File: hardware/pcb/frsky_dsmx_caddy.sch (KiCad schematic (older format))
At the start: 28 parts, among them P1 G9X, P2 Fr-Sky, P3 DSMX, Q1 BC847C, Q2 Si2319DS, Q3 Si2319DS, Q4 BC847C, U1 78L05, U2 LN-6206-30

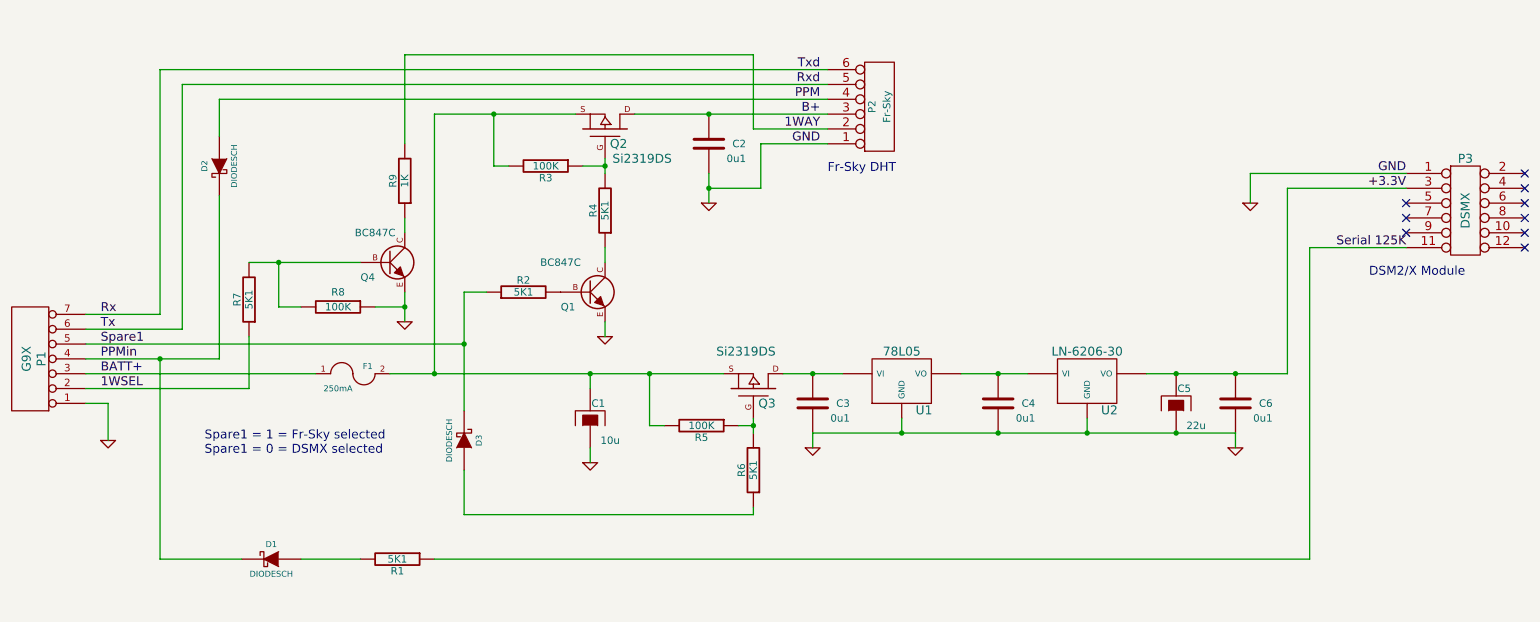
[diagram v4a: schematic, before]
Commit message: TX_caddy design fault corrected (and tested.)
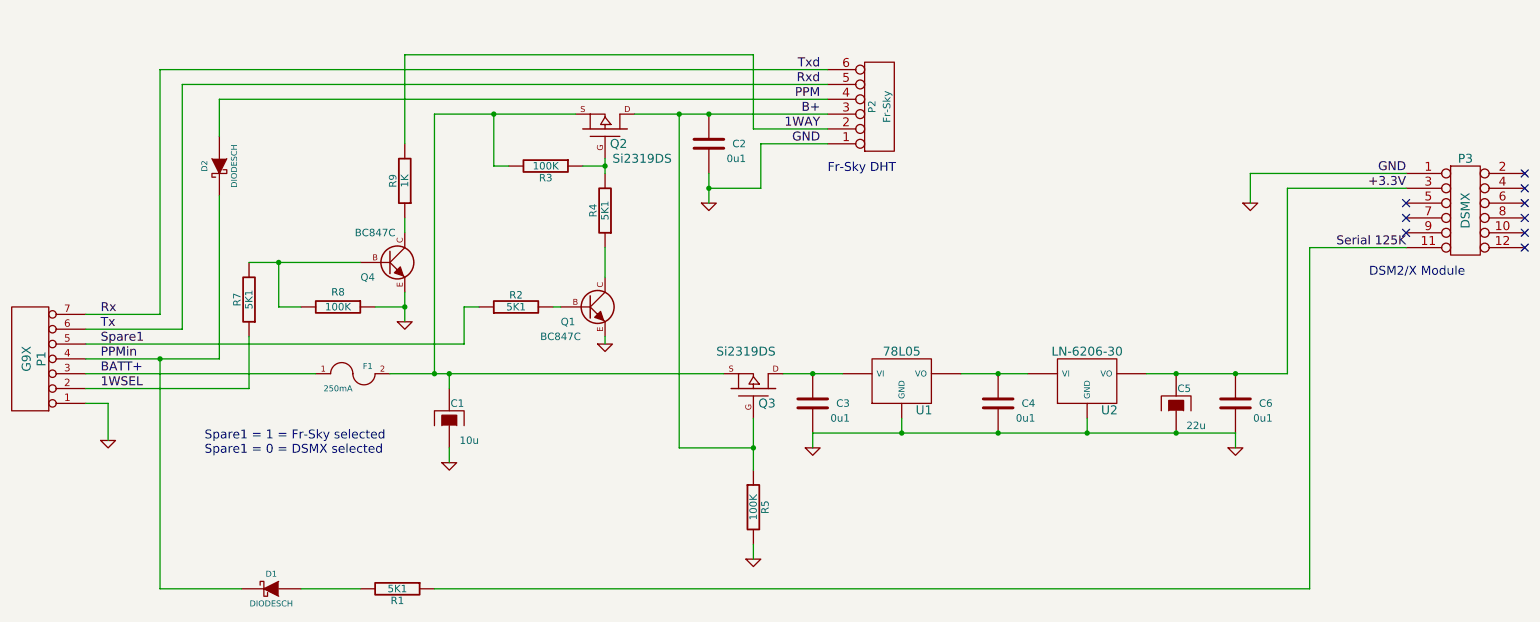
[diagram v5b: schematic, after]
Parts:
- removed D3: DIODESCH, symbol DIODESCH
- removed R6: 5K1, symbol R
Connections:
- net B+: now also Q3.G, R5.1
- net GND: now also R5.2
- net at C1.2, F1.2, Q2.S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: no longer R5.2
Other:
- moved on the sheet: C1, D1, Q1, R1, R2
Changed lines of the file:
@@
-EESchema Schematic File Version 2  date Wed 26 Sep 2012 04:29:42 PM NZST
+EESchema Schematic File Version 2  date Wed 24 Oct 2012 07:34:05 PM NZDT
 LIBS:gruvin
 LIBS:power
@@
 Sheet 1 1
 Title "Fr-Sky / DSMX TX Moudle Caddy"
-Date "26 sep 2012"
-Rev "1.2"
+Date "24 oct 2012"
+Rev "1.3"
 Comp ""
 Comment1 ""
@@
 Comment4 "Licensed under the TAPR Open Hardware License (see file,  LICENSE)"
 $EndDescr
-Text Label 1350 3600 0    60   ~ 0
-1WSEL
+Wire Wire Line
+	5750 4750 5750 4650
+Connection ~ 5250 1750
+Wire Wire Line
+	5250 1750 5250 4000
+Wire Wire Line
+	4750 2650 4750 2850
+Wire Wire Line
+	4750 3250 4750 3300
+Wire Wire Line
+	3800 3050 3800 3300
 Connection ~ 2550 2750
 Wire Wire Line
-	2550 3050 2550 2750
+	2550 2750 2550 3050
 Wire Wire Line
 	2550 3050 2700 3050
 Wire Wire Line
-	3100 2750 2350 2750
+	2350 2750 2550 2750
+Wire Wire Line
+	2550 2750 3100 2750
 Wire Wire Line
 	2350 3250 2350 3600
@@
 	2350 3600 1250 3600
 Wire Wire Line
-	3600 4750 9500 4750
-Wire Wire Line
-	9500 4750 9500 2650
+	3600 4950 9500 4950
+Wire Wire Line
+	9500 4950 9500 2650
 Wire Wire Line
 	9500 2650 10150 2650
-Connection ~ 3800 3300
-Wire Wire Line
-	3800 3750 3800 2950
-Wire Wire Line
-	3800 2950 3950 2950
-Wire Wire Line
-	1250 3300 3800 3300
-Wire Wire Line
-	5450 2150 5450 2350
+Wire Wire Line
+	3800 3050 3900 3050
+Wire Wire Line
+	3800 3300 1250 3300
+Wire Wire Line
+	5450 2350 5450 2250
+Wire Wire Line
+	5450 2250 5450 2150
 Connection ~ 5450 2250
 Wire Wire Line
-	6150 3900 6150 4000
-Wire Wire Line
-	9000 3900 9000 4000
-Wire Wire Line
-	4650 4000 4650 4100
-Wire Wire Line
-	1750 4750 1750 3400
-Wire Wire Line
-	1750 4750 2300 4750
+	6150 4000 6150 3900
+Wire Wire Line
+	9000 4000 9000 3900
+Wire Wire Line
+	3700 4000 3700 4100
+Wire Wire Line
+	1750 3400 1750 4950
+Wire Wire Line
+	1750 4950 2300 4950
 Connection ~ 8600 3900
 Connection ~ 8600 3500
 Connection ~ 9000 3500
 Wire Wire Line
-	6150 3900 9000 3900
+	9000 3900 8600 3900
+Wire Wire Line
+	8600 3900 8000 3900
+Wire Wire Line
+	8000 3900 7400 3900
+Wire Wire Line
+	7400 3900 6750 3900
+Wire Wire Line
+	6750 3900 6150 3900
 Connection ~ 1750 3400
 Wire Wire Line
-	2150 3400 2150 2300
+	2150 2300 2150 3400
 Wire Wire Line
 	10150 2150 9100 2150
@@
 	9100 2150 9100 2350
 Wire Wire Line
-	4450 2950 4450 2950
-Wire Wire Line
-	4750 2750 4750 2650
-Wire Wire Line
 	6250 1450 1750 1450
 Wire Wire Line
@@
 Wire Wire Line
 	1250 3500 2800 3500
-Connection ~ 5750 3850
-Wire Wire Line
-	5650 3850 5750 3850
-Connection ~ 4650 3500
-Wire Wire Line
-	7600 3500 7150 3500
-Wire Wire Line
-	4650 3500 4650 3600
-Wire Wire Line
-	8400 3500 9350 3500
-Wire Wire Line
-	4550 1750 3600 1750
-Wire Wire Line
-	4750 2050 4750 2150
+Connection ~ 3700 3500
+Wire Wire Line
+	7150 3500 7400 3500
+Wire Wire Line
+	7400 3500 7600 3500
+Wire Wire Line
+	3700 3500 3700 3600
+Wire Wire Line
+	8400 3500 8600 3500
+Wire Wire Line
+	8600 3500 9000 3500
+Wire Wire Line
+	9000 3500 9350 3500
+Wire Wire Line
+	4550 1750 4000 1750
+Wire Wire Line
+	4000 1750 3600 1750
+Wire Wire Line
+	4750 2150 4750 2100
+Wire Wire Line
+	4750 2100 4750 2050
 Connection ~ 6750 3900
-Wire Wire Line
-	4750 3150 4750 3250
 Connection ~ 6150 3500
 Connection ~ 7400 3900
 Wire Wire Line
-	6250 1750 4950 1750
+	4950 1750 5250 1750
+Wire Wire Line
+	5250 1750 5450 1750
+Wire Wire Line
+	5450 1750 6250 1750
 Wire Wire Line
 	8000 3900 8000 3800
 Connection ~ 7400 3500
 Wire Wire Line
-	5750 3900 5750 3800
-Wire Wire Line
-	5750 4450 3800 4450
-Wire Wire Line
-	5750 4450 5750 4400
-Wire Wire Line
 	3600 1750 3600 3500
 Connection ~ 3600 3500
@@
 Connection ~ 4750 2100
 Wire Wire Line
-	3300 3500 5550 3500
-Wire Wire Line
 	6250 1650 2150 1650
 Wire Wire Line
-	1250 3400 2150 3400
+	2150 3400 1750 3400
+Wire Wire Line
+	1750 3400 1250 3400
 Wire Wire Line
 	6250 1550 1900 1550
@@
 	2150 1650 2150 1900
 Wire Wire Line
-	6350 3500 5950 3500
-Wire Wire Line
-	3100 4750 2700 4750
+	5950 3500 6150 3500
+Wire Wire Line
+	6150 3500 6350 3500
+Wire Wire Line
+	3100 4950 2700 4950
 Wire Wire Line
 	1250 3700 1400 3700
@@
 	5800 2250 5800 1950
 Wire Wire Line
-	5150 3850 5050 3850
-Wire Wire Line
-	5050 3850 5050 3500
-Connection ~ 5050 3500
-Wire Wire Line
 	4100 2100 4000 2100
 Wire Wire Line
@@
 Connection ~ 4000 1750
 Wire Wire Line
-	3800 4450 3800 4150
-Wire Wire Line
 	5800 1950 6250 1950
 Wire Wire Line
-	3400 2950 3400 3150
+	3400 3150 3400 3050
+Wire Wire Line
+	3400 3050 3400 2950
 Wire Wire Line
 	3400 2550 3400 2450
@@
 	3200 3050 3400 3050
 Connection ~ 3400 3050
+Wire Wire Line
+	5550 3500 3700 3500
+Wire Wire Line
+	3700 3500 3600 3500
+Wire Wire Line
+	3600 3500 3300 3500
+Wire Wire Line
+	4450 3050 4400 3050
+Wire Wire Line
+	5750 4150 5750 4000
+Wire Wire Line
+	5750 4000 5750 3800
+Wire Wire Line
+	5250 4000 5750 4000
+Connection ~ 5750 4000
+$Comp
+L GND #PWR?
+U 1 1 50878285
+P 5750 4750
+F 0 "#PWR?" H 5750 4750 30  0001 C CNN
+F 1 "GND" H 5750 4680 30  0001 C CNN
+	1    5750 4750
+	1    0    0    -1
+$EndComp
+$Comp
+L R R5
+U 1 1 50877F34
+P 5750 4400
+F 0 "R5" V 5830 4400 50  0000 C CNN
+F 1 "100K" V 5750 4400 50  0000 C CNN
+	1    5750 4400
+	1    0    0    -1
+$EndComp
+Text Label 1350 3600 0    60   ~ 0
+1WSEL
 $Comp
 L BC847C Q4
@@
 $EndComp
 $Comp
-L GND #PWR01
+L GND #PWR2
 U 1 1 50627C0D
 P 3400 3150
-F 0 "#PWR01" H 3400 3150 30  0001 C CNN
+F 0 "#PWR2" H 3400 3150 30  0001 C CNN
 F 1 "GND" H 3400 3080 30  0001 C CNN
 	1    3400 3150
@@
 NoConn ~ 10150 2550
 $Comp
-L GND #PWR02
+L GND #PWR8
 U 1 1 504D1983
 P 9000 4000
-F 0 "#PWR02" H 9000 4000 30  0001 C CNN
+F 0 "#PWR8" H 9000 4000 30  0001 C CNN
 F 1 "GND" H 9000 3930 30  0001 C CNN
 	1    9000 4000
@@
 $EndComp
 $Comp
-L GND #PWR03
+L GND #PWR3
 U 1 1 504D1897
-P 4650 4100
-F 0 "#PWR03" H 4650 4100 30  0001 C CNN
-F 1 "GND" H 4650 4030 30  0001 C CNN
-	1    4650 4100
+P 3700 4100
+F 0 "#PWR3" H 3700 4100 30  0001 C CNN
+F 1 "GND" H 3700 4030 30  0001 C CNN
+	1    3700 4100
 	1    0    0    -1
 $EndComp
@@
 L DIODESCH D1
 U 1 1 504D150C
-P 2500 4750
-F 0 "D1" H 2500 4850 40  0000 C CNN
-F 1 "DIODESCH" H 2500 4650 40  0000 C CNN
-	1    2500 4750
+P 2500 4950
+F 0 "D1" H 2500 5050 40  0000 C CNN
+F 1 "DIODESCH" H 2500 4850 40  0000 C CNN
+	1    2500 4950
 	-1   0    0    -1
 $EndComp
@@
 L R R1
 U 1 1 504D1401
-P 3350 4750
-F 0 "R1" V 3430 4750 50  0000 C CNN
-F 1 "5K1" V 3350 4750 50  0000 C CNN
-	1    3350 4750
+P 3350 4950
+F 0 "R1" V 3430 4950 50  0000 C CNN
+F 1 "5K1" V 3350 4950 50  0000 C CNN
+	1    3350 4950
 	0    1    1    0
 $EndComp
 $Comp
-L GND #PWR04
+L GND #PWR9
 U 1 1 504D13B3
 P 9100 2350
-F 0 "#PWR04" H 9100 2350 30  0001 C CNN
+F 0 "#PWR9" H 9100 2350 30  0001 C CNN
 F 1 "GND" H 9100 2280 30  0001 C CNN
 	1    9100 2350
@@
 PPMin
 $Comp
-L GND #PWR05
+L GND #PWR5
 U 1 1 504D1165
 P 5450 2350
-F 0 "#PWR05" H 5450 2350 30  0001 C CNN
+F 0 "#PWR5" H 5450 2350 30  0001 C CNN
 F 1 "GND" H 5450 2280 30  0001 C CNN
 	1    5450 2350
@@
 BATT+
 $Comp
-L GND #PWR06
+L GND #PWR1
 U 1 1 504D1086
 P 1400 3950
-F 0 "#PWR06" H 1400 3950 30  0001 C CNN
+F 0 "#PWR1" H 1400 3950 30  0001 C CNN
 F 1 "GND" H 1400 3880 30  0001 C CNN
 	1    1400 3950
@@
 	1    3050 3500
 	1    0    0    -1
-$EndComp
-$Comp
-L R R5
-U 1 1 504D0D5C
-P 5400 3850
-F 0 "R5" V 5480 3850 50  0000 C CNN
-F 1 "100K" V 5400 3850 50  0000 C CNN
-	1    5400 3850
-	0    1    1    0
 $EndComp
 $Comp
@@
 $EndComp
 $Comp
-L R R6
-U 1 1 504D0D5A
-P 5750 4150
-F 0 "R6" V 5830 4150 50  0000 C CNN
-F 1 "5K1" V 5750 4150 50  0000 C CNN
-	1    5750 4150
-	-1   0    0    1
-$EndComp
-$Comp
 L CAPAPOL C1
 U 1 1 504D0AFE
-P 4650 3800
-F 0 "C1" H 4550 3700 50  0000 L CNN
-F 1 "10u" H 4450 3950 50  0000 L CNN
-	1    4650 3800
+P 3700 3800
+F 0 "C1" H 3600 3700 50  0000 L CNN
+F 1 "10u" H 3500 3950 50  0000 L CNN
+	1    3700 3800
 	-1   0    0    1
 $EndComp
@@
 $EndComp
 $Comp
-L DIODESCH D3
-U 1 1 504D08BE
-P 3800 3950
-F 0 "D3" H 3800 4050 40  0000 C CNN
-F 1 "DIODESCH" H 3800 3850 40  0000 C CNN
-	1    3800 3950
-	0    1    -1   0
-$EndComp
-$Comp
-L GND #PWR07
+L GND #PWR4
 U 1 1 4E7B4B20
-P 4750 3250
-F 0 "#PWR07" H 4750 3250 30  0001 C CNN
-F 1 "GND" H 4750 3180 30  0001 C CNN
-	1    4750 3250
+P 4750 3300
+F 0 "#PWR4" H 4750 3300 30  0001 C CNN
+F 1 "GND" H 4750 3230 30  0001 C CNN
+	1    4750 3300
 	1    0    0    -1
 $EndComp
@@
 L R R2
 U 1 1 4E7B4AFA
-P 4200 2950
-F 0 "R2" V 4280 2950 50  0000 C CNN
-F 1 "5K1" V 4200 2950 50  0000 C CNN
-	1    4200 2950
+P 4150 3050
+F 0 "R2" V 4230 3050 50  0000 C CNN
+F 1 "5K1" V 4150 3050 50  0000 C CNN
+	1    4150 3050
 	0    -1   -1   0
 $EndComp
@@
 L BC847C Q1
 U 1 1 4E7B4ABC
-P 4650 2950
-F 0 "Q1" H 4500 2850 50  0000 C CNN
-F 1 "BC847C" H 4450 3150 50  0000 C CNN
-F 2 "SOT23-BCE" H 4840 2950 30  0001 C CNN
-	1    4650 2950
+P 4650 3050
+F 0 "Q1" H 4500 2950 50  0000 C CNN
+F 1 "BC847C" H 4450 2850 50  0000 C CNN
+F 2 "SOT23-BCE" H 4840 3050 30  0001 C CNN
+	1    4650 3050
 	1    0    0    -1
 $EndComp
@@
 $EndComp
 $Comp
-L GND #PWR08
+L GND #PWR7
 U 1 1 4E1493B8
 P 6150 4000
-F 0 "#PWR08" H 6150 4000 30  0001 C CNN
+F 0 "#PWR7" H 6150 4000 30  0001 C CNN
 F 1 "GND" H 6150 3930 30  0001 C CNN
 	1    6150 4000
